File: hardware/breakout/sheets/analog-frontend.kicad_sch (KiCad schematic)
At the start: 134 parts, among them J19 ACCES I/O USB-AO16-8A mating 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, J20 Photodiode 1 (passive, coax, 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, J21 Photodiode 2 (passive, coax, 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, J22 Microphone (battery-powered, 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, J23 Ambient light sensor (battery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, J24 Accelerometer motion energy (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, J25 Joystick X (battery-powered, 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, J26 Joystick Y (battery-powered, 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, J27 Misc analog input 1 (panel BN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, J28 Misc analog input 1 (panel BN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, J29 Misc analog input 2 (panel BN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, J30 Misc analog input 2 (panel BN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, J31 Misc analog input 3 (panel BN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, J32 Misc analog input 3 (panel BN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, U16 INA105KU, U17 INA105KU, U18 INA105KU, U19 INA105KU, U20 INA105KU, U21 INA105KU, U22 OPA2197IDR, U23 OPA4197IDR, U24 INA105KU, U25 INA105KU, U26 INA105KU, U27 INA105KU, U28 INA105KU, U29 INA105KU, U30 INA105KU

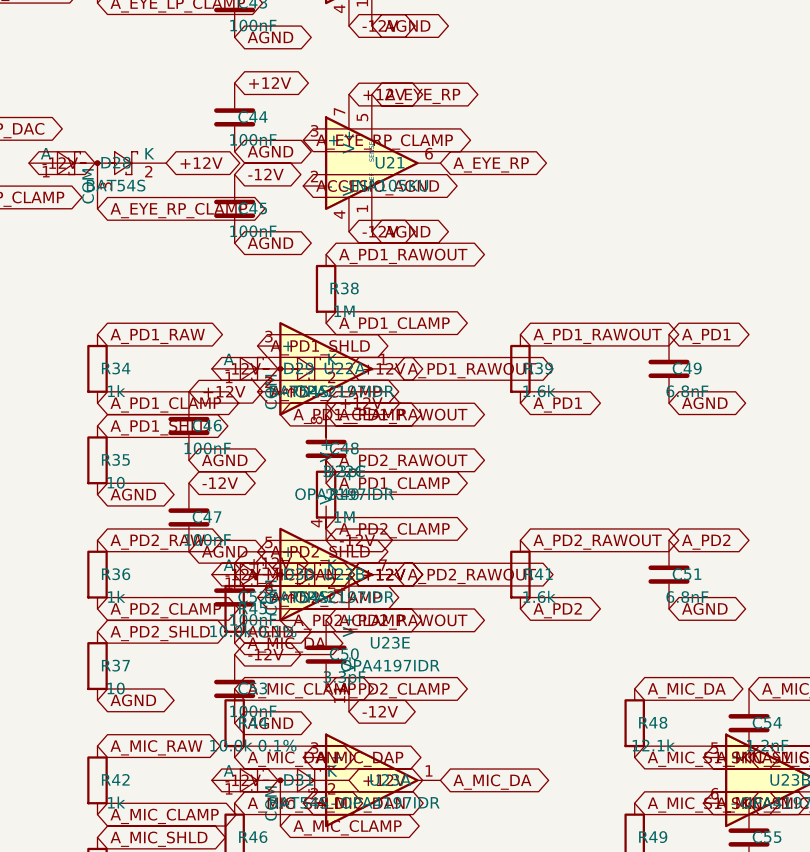
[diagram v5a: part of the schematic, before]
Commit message: fix(hardware): the analog front-end corrections (F3, M1, M2, M4; D1 recorded)
Five findings, both photodiode channels each.

F3 -- THE TRANSIMPEDANCE STAGE SATURATED. R38/R40 1M -> 180k. An FDS100 is
13 mm2 at 0.30 A/W, so a display flip patch at ~0.29 mW/cm2 delivers
~11.3 uA -- and 11.3 uA x 1M demands 11.3 V, twice this board's +-5 V analog
convention and past both NI's and Intan's input range. The stage clipped
long before full scale.

That matters more than a gain error sounds. The flat part is the BRIGHT
part, and the edge these channels exist to time is what survives, so the
defect would have looked like "it works" on a scope. 180k puts peak white
near 2.0 V, which also lands inside the DAC's own 0-2.048 V span after D1.

The DNP parallel trim positions the finding asks for are fitted (R196/R197,
unpopulated). A resistor pad rather than a jumper, deliberately: gain rests
on an estimate of display irradiance rather than a measurement, so bring-up
needs a way to move it, but a mechanical contact at a 180k summing junction
would be a leakage and noise liability.

M1 -- IT WAS ALSO UNDER-COMPENSATED. C48/C50 3.3pF -> 22pF. 3.3pF was
fitted for a 1M stage against an assumed 300-500 pF of input capacitance.
Thorlabs publish the FDS100's capacitance only at 20 V bias (24 pF); this
design is forced into ZERO bias by the no-power-in-the-booth constraint,
where it is at maximum and unpublished -- estimated 130-380 pF, and 440-900
pF with 3-5 m of coax.

22pF at 180k is deliberate over-compensation, not a fit: stable to 5.5 nF
of input capacitance (~50 m of coax) at -3 dB = 40 kHz, still four times
what these channels need. The stage stops depending on cable length and on
a diode capacitance nobody can look up. The BOM now calls for C0G/NP0 on
these two rather than X7R -- a compensation capacitor whose value moves
with bias or temperature is not doing this job.

M2 -- THE MUX TAPPED THE WRONG NODE. The eight muxes' S7/S8 inputs move
from A_PD1/A_PD2 to A_PD1_NI_BUF/A_PD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
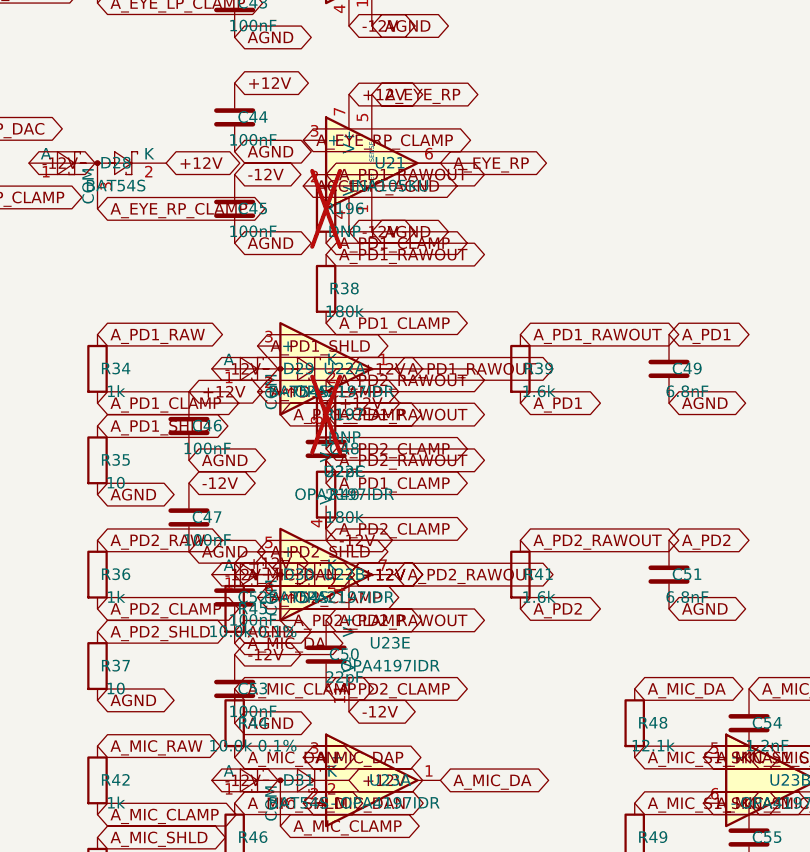
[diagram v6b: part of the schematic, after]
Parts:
- added R196, R197: DNP, Resistor_SMD:R_0603_1608Metric, symbol Device:R
- C48, C50: value 3.3pF -> 22pF
- R38, R40: value 1M -> 180k
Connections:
- net A_PD1_CLAMP: now also R196.2
- net A_PD1_RAWOUT: now also R196.1
- net A_PD2_CLAMP: now also R197.2
- net A_PD2_RAWOUT: now also R197.1
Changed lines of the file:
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@@
 			(effects (font (size 1.27 1.27)))
 		)
-		(property "Value" "1M"
+		(property "Value" "180k"
 			(at 92.202 151.12999999999997 0)
 			(effects (font (size 1.27 1.27)))
@@
 			(effects (font (size 1.27 1.27)))
 		)
-		(property "Value" "3.3pF"
+		(property "Value" "22pF"
 			(at 92.202 168.91 0)
 			(effects (font (size 1.27 1.27)))
@@
 		(property "Intersheetrefs" "${INTERSHEET_REFS}"
 			(at 90.17 170.18 0)
+			(effects (font (size 1.27 1.27)) (hide yes))
+		)
+	)
+	(symbol
+		(lib_id "Device:R")
+		(at 90.17 139.7 0)
+		(unit 1)
+		(exclude_from_sim no)
+		(in_bom yes)
+		(on_board yes)
+		(dnp yes)
+		(property "Reference" "R196"
+			(at 92.202 139.7 0)
+			(effects (font (size 1.27 1.27)))
+		)
+		(property "Value" "DNP"
+			(at 92.202 142.23999999999998 0)
+			(effects (font (size 1.27 1.27)))
+		)
+		(property "Footprint" "Resistor_SMD:R_0603_1608Metric"
+			(at 90.17 139.7 0)
+			(effects (font (size 1.27 1.27)) (hide yes))
+		)
+		(property "Datasheet" ""
+			(at 90.17 139.7 0)
+			(effects (font (size 1.27 1.27)) (hide yes))
+		)
+		(pin "1")
+		(pin "2")
+		(instances
+			(project "breakout"
+				(path "/d2c4d978-5db4-46d9-a1cd-a7af0aeb1700/224d9c0c-248e-4691-aa68-8b342525837c"
+					(reference "R196") (unit 1)
+				)
+			)
+		)
+	)
+	(global_label "A_PD1_RAWOUT"
+		(shape bidirectional)
+		(at 90.17 135.89 0)
+		(effects (font (size 1.27 1.27)) (justify left))
+		(property "Intersheetrefs" "${INTERSHEET_REFS}"
+			(at 90.17 135.89 0)
+			(effects (font (size 1.27 1.27)) (hide yes))
+		)
+	)
+	(global_label "A_PD1_CLAMP"
+		(shape bidirectional)
+		(at 90.17 143.51 0)
+		(effects (font (size 1.27 1.27)) (justify left))
+		(property "Intersheetrefs" "${INTERSHEET_REFS}"
+			(at 90.17 143.51 0)
 			(effects (font (size 1.27 1.27)) (hide yes))
 		)
@@
 			(effects (font (size 1.27 1.27)))
 		)
-		(property "Value" "1M"
+		(property "Value" "180k"
 			(at 92.202 173.98999999999998 0)
 			(effects (font (size 1.27 1.27)))
@@
 			(effects (font (size 1.27 1.27)))
 		)
-		(property "Value" "3.3pF"
+		(property "Value" "22pF"
 			(at 92.202 191.76999999999995 0)
 			(effects (font (size 1.27 1.27)))
@@
 			(effects (font (size 1.27 1.27)) (hide yes))
 		)
+	)
+	(symbol
+		(lib_id "Device:R")
+		(at 90.17 162.55999999999997 0)
+		(unit 1)
+		(exclude_from_sim no)
+		(in_bom yes)
+		(on_board yes)
+		(dnp yes)
+		(property "Reference" "R197"
+			(at 92.202 162.55999999999997 0)
+			(effects (font (size 1.27 1.27)))
+		)
+		(property "Value" "DNP"
+			(at 92.202 165.09999999999997 0)
+			(effects (font (size 1.27 1.27)))
+		)
+		(property "Footprint" "Resistor_SMD:R_0603_1608Metric"
+			(at 90.17 162.55999999999997 0)
+			(effects (font (size 1.27 1.27)) (hide yes))
+		)
+		(property "Datasheet" ""
+			(at 90.17 162.55999999999997 0)
+			(effects (font (size 1.27 1.27)) (hide yes))
+		)
+		(pin "1")
+		(pin "2")
+		(instances
+			(project "breakout"
+				(path "/d2c4d978-5db4-46d9-a1cd-a7af0aeb1700/224d9c0c-248e-4691-aa68-8b342525837c"
+					(reference "R197") (unit 1)
+				)
+			)
+		)
+	)
+	(global_label "A_PD2_RAWOUT"
+		(shape bidirectional)
+		(at 90.17 158.74999999999997 0)
+		(effects (font (size 1.27 1.27)) (justify left))
+		(property "Intersheetrefs" "${INTERSHEET_REFS}"
+			(at 90.17 158.74999999999997 0)
+			(effects (font (size 1.27 1.27)) (hide yes))
+		)
+	)
+	(global_label "A_PD2_CLAMP"
+		(shape bidirectional)
+		(at 90.17 166.36999999999998 0)
+		(effects (font (size 1.27 1.27)) (justify left))
+		(property "Intersheetrefs" "${INTERSHEET_REFS}"
+			(at 90.17 166.36999999999998 0)
+			(effects (font (size 1.27 1.27)) (hide yes))
+		)
